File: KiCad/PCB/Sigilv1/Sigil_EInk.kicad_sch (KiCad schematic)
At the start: 4 parts, among them J2 INLAND E-PAPER HEADER (8-PIN), J3 BUZZER LOGICAL ONLY, J4 ANALOG JOYSTICK HEADER (5-PIN), U1 REMOVABLE ESP32 DEVKIT / 2 x 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

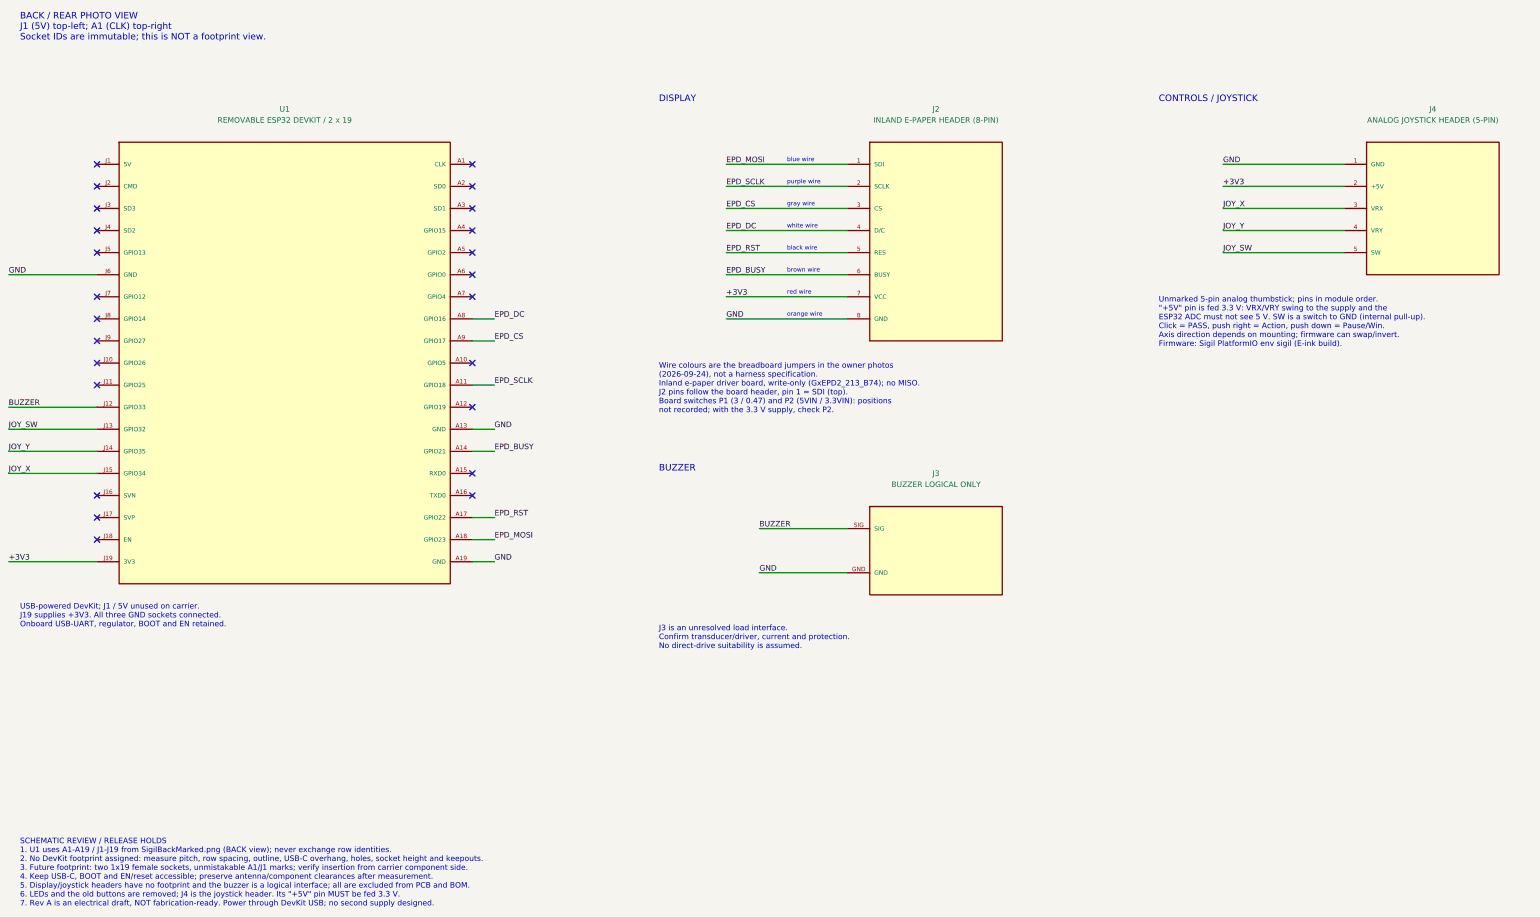
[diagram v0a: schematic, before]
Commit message: Sigil-rendered status light, Jewel ring, BOOT Pair; louder Atlas speaker
- LedState (packet 25, CAPABILITY_LED_STATE 0x20): Atlas sends the light's
  meaning (cue, overlays, seat, style, anchor age) once per change and on
  every Hello; the Sigil renders it (sigil_led.cpp) to an RGB LED (PWM on
  all pins) and, on the E-ink build, spatially on a NeoPixel Jewel 7 RGBW
  (Adafruit NeoPixel 1.15.5, GPIO26). Legacy SetRed/Green/Blue kept.
  LedCue/LedOverlay move to protocol.h.
- Pair is the DevKit BOOT button (GPIO0) on both hardware builds; Wokwi
  keeps GPIO19.
- Atlas speaker: LEDC square wave, volume steps ~1/2, 3/4, full.
- E-ink schematic gains J5 (Jewel) and R1; verifier checks the ring pin.
- Sigil 0.6.0-dev; host tests for the renderer and LedState transport.

Co-Authored-By: Claude Opus 5.5 <noreply@anthropic.com>
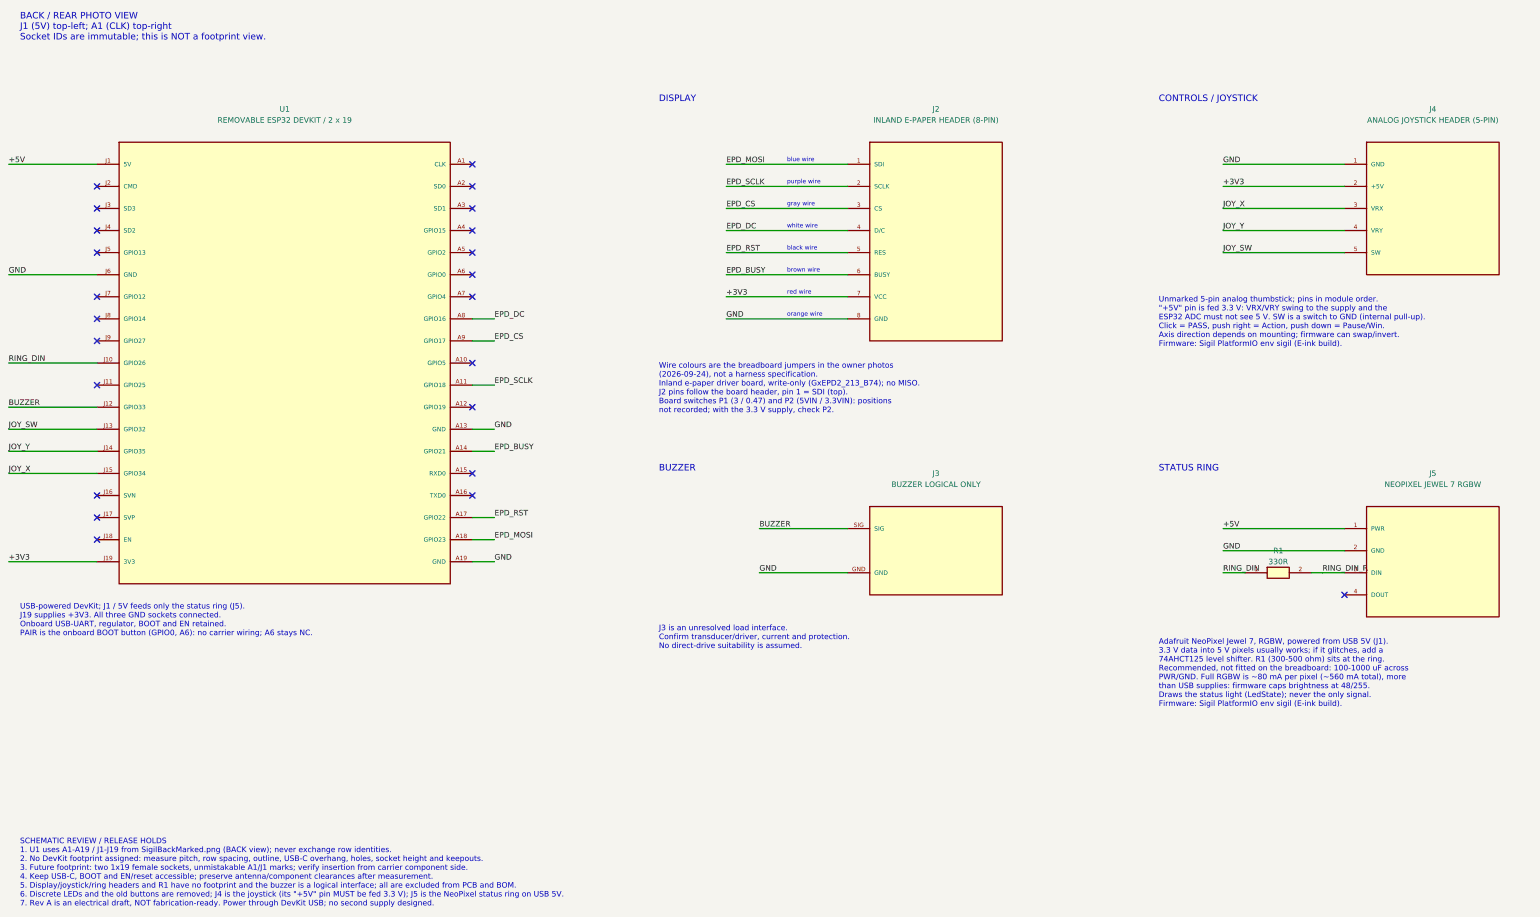
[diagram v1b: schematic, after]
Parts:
- added J5: NEOPIXEL JEWEL 7 RGBW, symbol Sigil:NeoPixel_Jewel7_RGBW
- added R1: 330R, symbol Sigil:Resistor_Series
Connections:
- net GND: now also J5.2 (GND)
- net +5V: now reaches U1.J1 (5V)
- net +5V: now also J5.1 (PWR)
- net RING_DIN: now reaches U1.J10 (GPIO26)
- net RING_DIN: now also R1.1
- new net RING_DIN_R: J5.3 (DIN), R1.2
- no-connect marks 24 -> 23
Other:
- note added: "Adafruit NeoPixel Jewel 7, RGBW, powered from USB 5V (J1). 3.3 V data into 5 V pixels usually works; if it glitches, add a 74AHCT125 level shifter. R1 (300-500 ohm) sits at the ring. Recommended, not fitted on the breadboard: 100-1000 uF across PWR/GND. Full RGBW is ~80 mA per pixel (~560 mA total), more than USB supplies: firmware caps brightness at 48/255. Draws the status light (LedState); nev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"
- note added: "STATUS RING"
- note added: "USB-powered DevKit; J1 / 5V feeds only the status ring (J5). J19 supplies +3V3. All three GND sockets connected. Onboard USB-UART, regulator, BOOT and EN retained. PAIR is the onboard BOOT button (GPIO0, A6): no carrier wiring; A6 stays NC."
- note removed: "USB-powered DevKit; J1 / 5V unused on carrier. J19 supplies +3V3. All three GND sockets connected. Onboard USB-UART, regulator, BOOT and EN retained."
